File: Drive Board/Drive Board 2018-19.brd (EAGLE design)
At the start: 379.8 x 115 mm, 77 parts, among them IC1 ACS758KCB, IC2 ACS758KCB, IC3 ACS758KCB, IC4 ACS758KCB, IC5 7812T, IC6 LM741P, K1 G5L, K2 G5L, K3 G5L

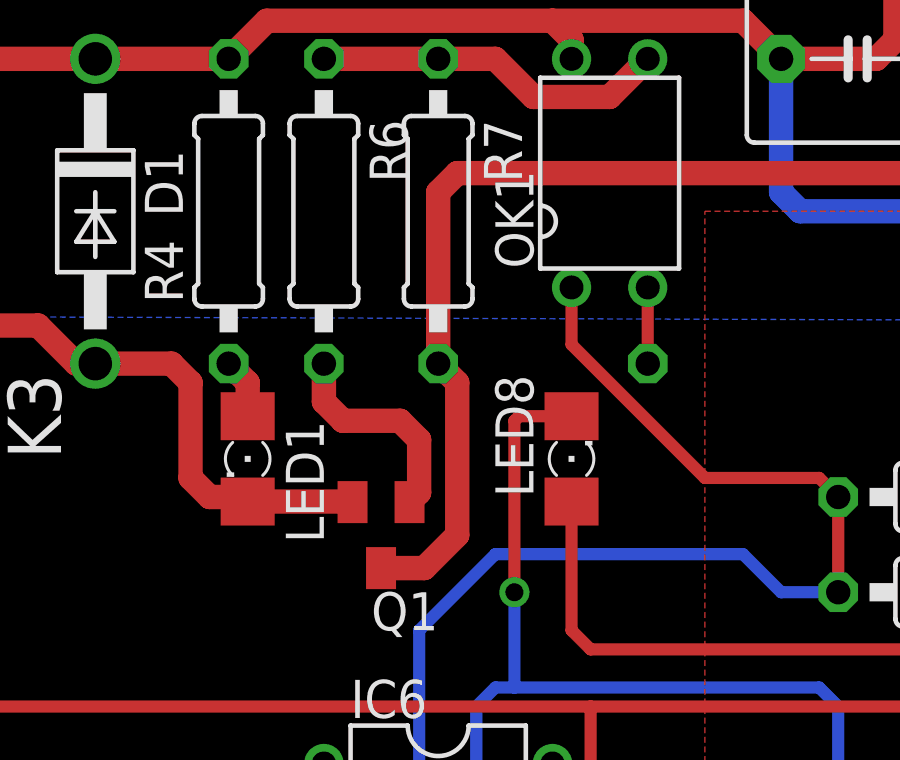
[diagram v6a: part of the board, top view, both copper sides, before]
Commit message: Fixed mixed ground signals
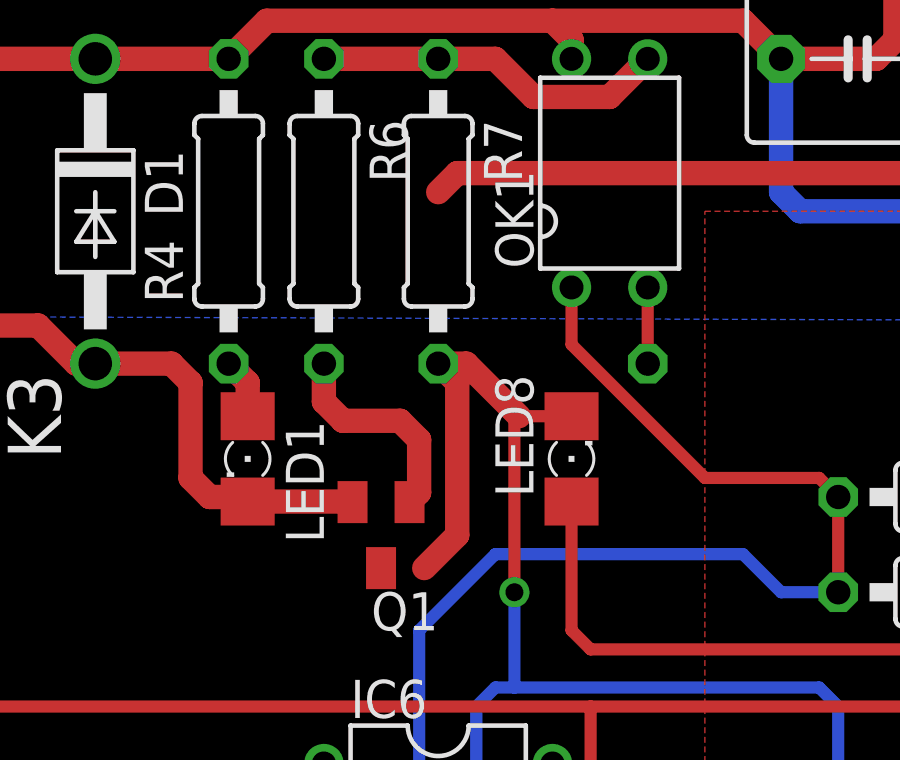
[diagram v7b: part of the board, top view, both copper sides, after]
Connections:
- removed net BATTERY_V-: C7.2, C8.2, IC5.2, Q1.3, R7.2
- net GND: now also C7.2, C8.2, IC5.2, Q1.3, R7.2
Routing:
- net BATTERY_V-: track 55.7 -> 0.00 mm
- net GND: track 300.1 -> 352.1 mm
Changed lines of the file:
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@@
 <wire x1="195.66" y1="92.67" x2="196.86" y2="94.78" width="0" layer="19" extent="1-1"/>
-</signal>
-<signal name="BATTERY_V-">
-<contactref element="Q1" pad="3"/>
-<contactref element="R7" pad="2"/>
-<contactref element="IC5" pad="2"/>
-<contactref element="C7" pad="2"/>
-<contactref element="C8" pad="2"/>
-<wire x1="159.385" y1="90.805" x2="156.845" y2="90.805" width="0.8128" layer="1"/>
-<wire x1="156.845" y1="90.805" x2="156.845" y2="87.63" width="0.8128" layer="1"/>
-<wire x1="156.845" y1="87.63" x2="156.21" y2="86.995" width="0.8128" layer="1"/>
-<wire x1="156.21" y1="86.995" x2="140.97" y2="86.995" width="0.8128" layer="1"/>
-<wire x1="140.97" y1="86.995" x2="140.335" y2="86.36" width="0.8128" layer="1"/>
-<wire x1="140.335" y1="86.36" x2="140.335" y2="80.645" width="0.8128" layer="1"/>
-<wire x1="159.385" y1="90.805" x2="159.385" y2="98.425" width="0.8128" layer="1"/>
-<wire x1="159.385" y1="98.425" x2="160.02" y2="99.06" width="0.8128" layer="1"/>
-<wire x1="160.02" y1="99.06" x2="166.37" y2="99.06" width="0.8128" layer="1"/>
-<wire x1="166.37" y1="99.06" x2="167.005" y2="98.425" width="0.8128" layer="1"/>
-<wire x1="167.005" y1="95.885" x2="167.005" y2="98.425" width="0.8128" layer="1"/>
-<wire x1="138.43" y1="73.83" x2="139.87" y2="73.83" width="0.8128" layer="1"/>
-<wire x1="139.87" y1="73.83" x2="140.97" y2="74.93" width="0.8128" layer="1"/>
-<wire x1="140.97" y1="74.93" x2="140.97" y2="80.01" width="0.8128" layer="1"/>
-<wire x1="140.97" y1="80.01" x2="140.335" y2="80.645" width="0.8128" layer="1"/>
 </signal>
 <signal name="OUTA1">
@@
 <contactref element="U$9" pad="P$2" route="any" routetag="G$1.CONTACT"/>
 <contactref element="U$9" pad="RIGHTHOLE" route="any" routetag="G$1.CONTACT"/>
+<contactref element="Q1" pad="3"/>
+<contactref element="R7" pad="2"/>
+<wire x1="139.87" y1="73.83" x2="140.97" y2="74.93" width="0.8128" layer="1"/>
+<wire x1="140.97" y1="74.93" x2="140.97" y2="80.01" width="0.8128" layer="1"/>
+<wire x1="140.97" y1="80.01" x2="140.335" y2="80.645" width="0.8128" layer="1"/>
+<contactref element="IC5" pad="2"/>
+<contactref element="C7" pad="2"/>
+<contactref element="C8" pad="2"/>
+<wire x1="159.385" y1="90.805" x2="156.845" y2="90.805" width="0.8128" layer="1"/>
+<wire x1="156.845" y1="90.805" x2="156.845" y2="87.63" width="0.8128" layer="1"/>
+<wire x1="156.845" y1="87.63" x2="156.21" y2="86.995" width="0.8128" layer="1"/>
+<wire x1="156.21" y1="86.995" x2="140.97" y2="86.995" width="0.8128" layer="1"/>
+<wire x1="140.97" y1="86.995" x2="140.335" y2="86.36" width="0.8128" layer="1"/>
+<wire x1="159.385" y1="90.805" x2="159.385" y2="98.425" width="0.8128" layer="1"/>
+<wire x1="159.385" y1="98.425" x2="160.02" y2="99.06" width="0.8128" layer="1"/>
+<wire x1="160.02" y1="99.06" x2="166.37" y2="99.06" width="0.8128" layer="1"/>
+<wire x1="166.37" y1="99.06" x2="167.005" y2="98.425" width="0.8128" layer="1"/>
+<wire x1="167.005" y1="95.885" x2="167.005" y2="98.425" width="0.8128" layer="1"/>
+<wire x1="140.335" y1="80.645" x2="141.274" y2="80.645" width="0.8128" layer="1"/>
+<wire x1="141.274" y1="80.645" x2="143.027" y2="78.892" width="0.8128" layer="1"/>
+<wire x1="139.87" y1="73.83" x2="138.43" y2="73.83" width="0" layer="19" extent="1-1"/>
+<wire x1="140.335" y1="86.36" x2="140.335" y2="80.645" width="0" layer="19" extent="1-1"/>
 </signal>
 <signal name="A5">
